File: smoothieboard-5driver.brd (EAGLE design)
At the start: 129.5 x 105.1 mm, 276 parts, among them IC1 LPC1769, IC10 LM1117-3.3V, IC11 78L12F, IC12 A4982, IC2 A4982, IC3 A4982, IC4 MCP44X1, IC5 A4982, IC6 A4982, IC9 MCP44X1, J10 POWER_JACKSMD, Q1 BSL207SP, Q10 SUD50P04-08-GE3, Q2 12MHz, Q3 25MHz, Q4 ZXMN4A06, Q5 AOT240L, Q6 AOT240L, Q7 AOT240L, Q8 ZXMN4A06, Q9 ZXMN4A06, U1 USD-SOCKETNEW, X14 USBPTH

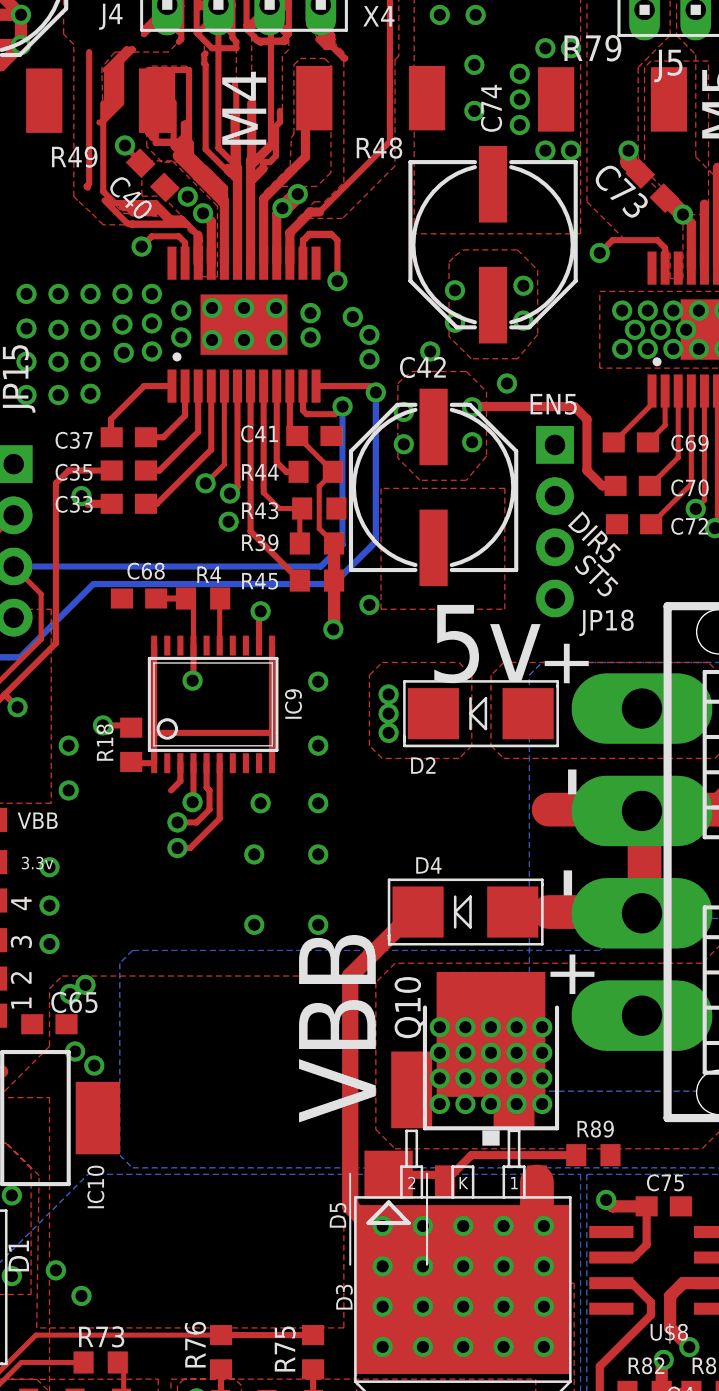
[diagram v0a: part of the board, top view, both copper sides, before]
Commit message: added footprint for optional R-78E-5.0 dc-dc converter for converting from VBB to 5V
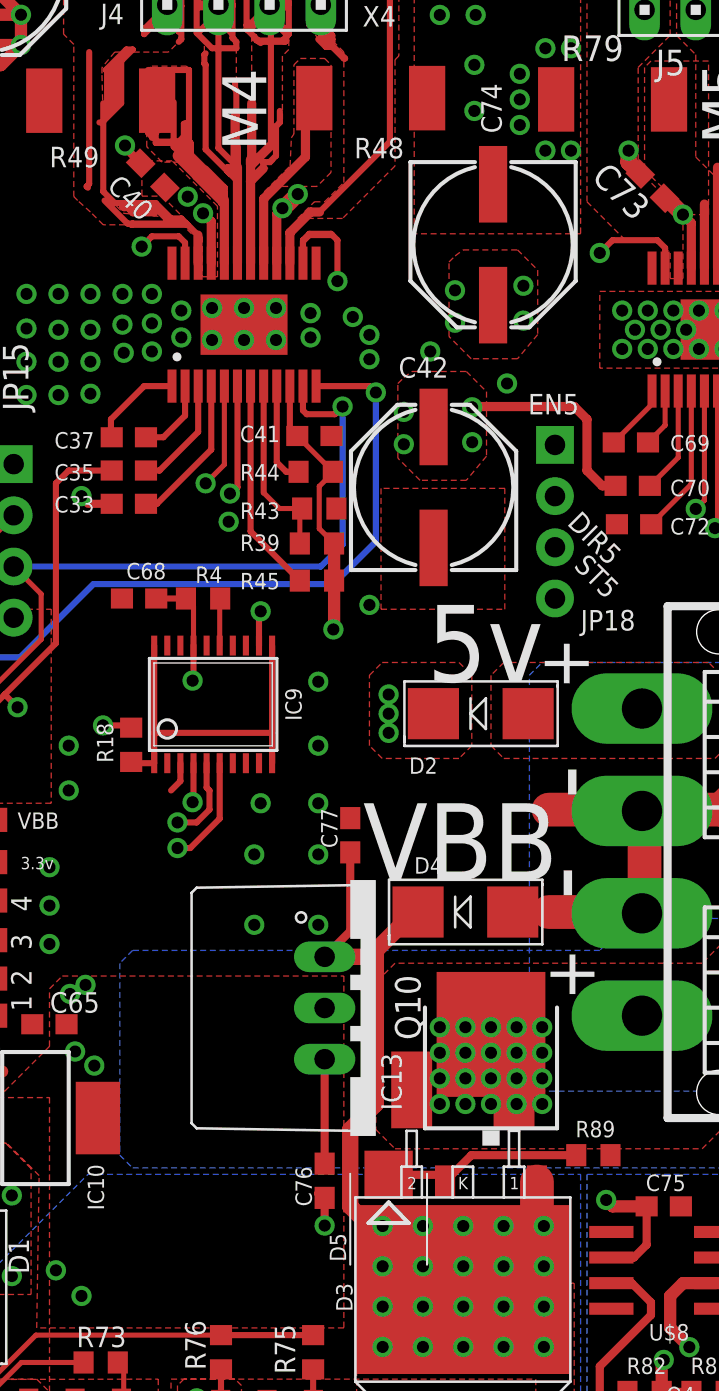
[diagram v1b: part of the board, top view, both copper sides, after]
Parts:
- added C76: .1uF, rcl:C0603
- added C77: .33uF, rcl:C0603
- added IC13: R-78E-5.0, logxen:R-78
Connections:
- net 5V: now also C76.1, IC13.3
- net GND: now also C76.2, C77.2, IC13.2
- net VBB: now also C77.1, IC13.1
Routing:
- net VBB: track 297.7 -> 306.1 mm
- net 5V: track 129.6 -> 137.8 mm
- net GND: track 286.5 -> 288.6 mm, vias 330 -> 331
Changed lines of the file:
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@@
 <?xml version="1.0" encoding="utf-8"?>
 <!DOCTYPE eagle SYSTEM "eagle.dtd">
-<eagle version="6.2">
+<eagle version="6.3">
 <drawing>
 <settings>
@@
 <grid distance="12.5" unitdist="mil" unit="mil" style="dots" multiple="8" display="no" altdistance="6.25" altunitdist="mil" altunit="mil"/>
 <layers>
-<layer number="1" name="Top" color="4" fill="1" visible="no" active="yes"/>
+<layer number="1" name="Top" color="4" fill="1" visible="yes" active="yes"/>
 <layer number="2" name="Route2" color="2" fill="1" visible="no" active="yes"/>
 <layer number="3" name="Route3" color="4" fill="3" visible="no" active="no"/>
@@
 <layer number="110" name="fp0" color="7" fill="1" visible="no" active="yes"/>
 <layer number="111" name="LPC17xx" color="7" fill="1" visible="no" active="yes"/>
+<layer number="112" name="tSilk" color="7" fill="1" visible="yes" active="yes"/>
 <layer number="116" name="Patch_BOT" color="9" fill="4" visible="no" active="yes"/>
 <layer number="121" name="_tsilk" color="7" fill="1" visible="yes" active="yes"/>
@@
 <layer number="124" name="bTestmark" color="7" fill="1" visible="no" active="yes"/>
 <layer number="125" name="_tNames" color="7" fill="1" visible="no" active="yes"/>
+<layer number="126" name="_bNames" color="7" fill="1" visible="yes" active="yes"/>
+<layer number="127" name="_tValues" color="7" fill="1" visible="yes" active="yes"/>
+<layer number="128" name="_bValues" color="7" fill="1" visible="yes" active="yes"/>
 <layer number="131" name="tAdjust" color="7" fill="1" visible="no" active="yes"/>
 <layer number="132" name="bAdjust" color="7" fill="1" visible="no" active="yes"/>
 <layer number="144" name="Drill_legend" color="7" fill="1" visible="no" active="yes"/>
 <layer number="151" name="HeatSink" color="7" fill="1" visible="no" active="yes"/>
+<layer number="152" name="_bDocu" color="7" fill="1" visible="yes" active="yes"/>
 <layer number="199" name="Contour" color="7" fill="1" visible="no" active="yes"/>
 <layer number="200" name="200bmp" color="1" fill="10" visible="no" active="yes"/>
@@
 <layer number="223" name="223bmp" color="24" fill="1" visible="no" active="no"/>
 <layer number="224" name="224bmp" color="25" fill="1" visible="no" active="no"/>
+<layer number="248" name="Housing" color="7" fill="1" visible="yes" active="yes"/>
+<layer number="249" name="Edge" color="7" fill="1" visible="yes" active="yes"/>
 <layer number="250" name="Descript" color="3" fill="1" visible="no" active="no"/>
 <layer number="251" name="SMDround" color="12" fill="11" visible="no" active="no"/>
@@
 <text x="107.886" y="68.255" size="1.016" layer="25" ratio="16" rot="R315">ST5</text>
 <text x="100.6475" y="62.5475" size="3.81" layer="121" ratio="16">5v</text>
-<text x="98.1075" y="40.64" size="3.81" layer="121" ratio="16" rot="R90">VBB</text>
+<text x="97.4725" y="52.705" size="3.81" layer="121" ratio="16">VBB</text>
 <text x="80.3275" y="55.245" size="0.8128" layer="121" ratio="16">VBB</text>
 <text x="18.0975" y="8.89" size="0.8128" layer="122" ratio="16" rot="MR270">5V</text>
@@
 </class>
 </classes>
-<designrules>
+<designrules name="default">
 <description language="de">&lt;b&gt;EAGLE Design Rules&lt;/b&gt;
 &lt;p&gt;
@@
 </element>
 <element name="D5" library="diode" package="SMB" value="15v" x="98.7425" y="35.8775" smashed="yes" rot="R270">
-<attribute name="NAME" x="95.8215" y="36.7665" size="0.8128" layer="25" rot="R270"/>
+<attribute name="NAME" x="95.8215" y="35.179" size="0.8128" layer="25" rot="R270"/>
 <attribute name="VALUE" x="95.3135" y="38.0365" size="1.27" layer="27" rot="R270"/>
 </element>
@@
 <attribute name="VALUE" x="75.8825" y="31.75" size="1.27" layer="27" rot="R180"/>
 </element>
+<element name="IC13" library="logxen" package="R-78" value="R-78E-5.0" x="98.1075" y="46.355" smashed="yes" rot="R270">
+<attribute name="NAME" x="99.3902" y="41.275" size="1.016" layer="25" ratio="10" rot="R90"/>
+<attribute name="VALUE" x="89.2175" y="52.705" size="1.27" layer="27" ratio="10"/>
+</element>
+<element name="C76" library="rcl" package="C0603" value=".1uF" x="95.5675" y="37.7825" smashed="yes" rot="R270">
+<attribute name="NAME" x="94.9325" y="36.5125" size="0.8128" layer="25" rot="R90"/>
+<attribute name="VALUE" x="93.6625" y="38.4175" size="1.27" layer="27" rot="R270"/>
+</element>
+<element name="C77" library="rcl" package="C0603" value=".33uF" x="96.8375" y="54.9275" smashed="yes" rot="R90">
+<attribute name="NAME" x="96.2025" y="54.2925" size="0.8128" layer="25" rot="R90"/>
+<attribute name="VALUE" x="98.7425" y="54.2925" size="1.27" layer="27" rot="R90"/>
+</element>
 </elements>
 <signals>
@@
 <contactref element="JP33" pad="5"/>
 <wire x1="76.975" y1="31.115" x2="74.6125" y2="31.115" width="0.8128" layer="15"/>
-<wire x1="86.43885625" y1="88.275940625" x2="85.6615" y2="89.154" width="0.254" layer="1"/>
+<contactref element="IC13" pad="2"/>
+<contactref element="C77" pad="2"/>
+<contactref element="C76" pad="2"/>
+<wire x1="86.43885625" y1="88.275940625" x2="85.6615" y2="89.053296875" width="0.4064" layer="1"/>
+<wire x1="85.6615" y1="89.053296875" x2="85.6615" y2="89.154" width="0.4064" layer="1"/>
+<wire x1="95.5675" y1="36.9325" x2="95.3525" y2="37.1475" width="0.4064" layer="1"/>
+<wire x1="95.3525" y1="37.1475" x2="95.25" y2="37.1475" width="0.4064" layer="1"/>
+<wire x1="95.25" y1="37.1475" x2="95.5675" y2="36.83" width="0.4064" layer="1"/>
+<wire x1="95.5675" y1="36.83" x2="95.5675" y2="35.56" width="0.4064" layer="1"/>
+<via x="95.5675" y="35.56" extent="1-16" drill="0.6"/>
 </signal>
 <signal name="3.3V">
@@
 <contactref element="D4" pad="C"/>
 <wire x1="100.203" y1="51.1175" x2="100.0125" y2="51.1175" width="0.8128" layer="1"/>
-<wire x1="100.0125" y1="51.1175" x2="96.8375" y2="47.9425" width="0.8128" layer="1"/>
-<wire x1="96.8375" y1="47.9425" x2="96.8375" y2="36.51" width="0.8128" layer="1"/>
+<wire x1="100.0125" y1="51.1175" x2="98.1075" y2="49.2125" width="0.8128" layer="1"/>
+<wire x1="98.1075" y1="49.2125" x2="98.1075" y2="41.5925" width="0.8128" layer="1"/>
+<wire x1="98.1075" y1="41.5925" x2="96.8375" y2="40.3225" width="0.8128" layer="1"/>
+<wire x1="96.8375" y1="40.3225" x2="96.8375" y2="36.51" width="0.8128" layer="1"/>
 <contactref element="Q10" pad="2"/>
 <contactref element="D5" pad="A"/>
@@
 <wire x1="98.445" y1="35.5375" x2="97.81" y2="35.5375" width="0.8128" layer="1"/>
 <wire x1="97.81" y1="35.5375" x2="96.8375" y2="36.51" width="0.8128" layer="1"/>
+<contactref element="IC13" pad="1"/>
+<contactref element="C77" pad="1"/>
+<wire x1="96.8375" y1="54.0775" x2="96.8375" y2="50.165" width="0.4064" layer="1"/>
+<wire x1="96.8375" y1="50.165" x2="95.5675" y2="48.895" width="0.4064" layer="1"/>
+<wire x1="98.1075" y1="49.2125" x2="97.79" y2="48.895" width="0.8128" layer="1"/>
+<wire x1="97.79" y1="48.895" x2="95.5675" y2="48.895" width="0.8128" layer="1"/>
 </signal>
 <signal name="P0W">
@@
 <wire x1="87.249" y1="89.281" x2="88.4555" y2="89.281" width="0.3048" layer="1"/>
 <wire x1="88.4555" y1="89.281" x2="88.519" y2="89.2175" width="0.3048" layer="1"/>
-<wire x1="86.9315" y1="89.916" x2="86.995" y2="90.2335" width="0.254" layer="1"/>
+<wire x1="86.9315" y1="89.916" x2="86.9315" y2="90.17" width="0.4064" layer="1"/>
 </signal>
 <signal name="N$48">
@@
 <vertex x="97.79" y="62.865"/>
 </polygon>
-<wire x1="93.6625" y1="60.325" x2="93.6625" y2="37.689" width="0.8128" layer="15"/>
+<wire x1="93.6625" y1="60.325" x2="93.6625" y2="44.45" width="0.8128" layer="15"/>
+<wire x1="93.6625" y1="44.45" x2="93.6625" y2="43.18" width="0.8128" layer="15"/>
+<wire x1="93.6625" y1="43.18" x2="93.6625" y2="37.689" width="0.8128" layer="15"/>
 <wire x1="93.6625" y1="37.689" x2="93.0275" y2="37.054" width="0.8128" layer="15"/>
 <wire x1="93.0275" y1="37.054" x2="80.046" y2="37.054" width="0.8128" layer="15"/>
@@
 <wire x1="16.637" y1="10.6045" x2="16.637" y2="8.118" width="0.6096" layer="16"/>
 <wire x1="16.637" y1="8.118" x2="16.504" y2="7.985" width="0.6096" layer="16"/>
+<contactref element="IC13" pad="3"/>
+<contactref element="C76" pad="1"/>
+<wire x1="95.5675" y1="38.6325" x2="95.5675" y2="43.815" width="0.4064" layer="1"/>
+<wire x1="94.2975" y1="43.815" x2="93.6625" y2="43.18" width="0.8128" layer="15"/>
+<wire x1="95.5675" y1="43.815" x2="94.2975" y2="43.815" width="0.8128" layer="15"/>
+<wire x1="94.2975" y1="43.815" x2="93.6625" y2="44.45" width="0.8128" layer="15"/>
 </signal>
 <signal name="+5V">

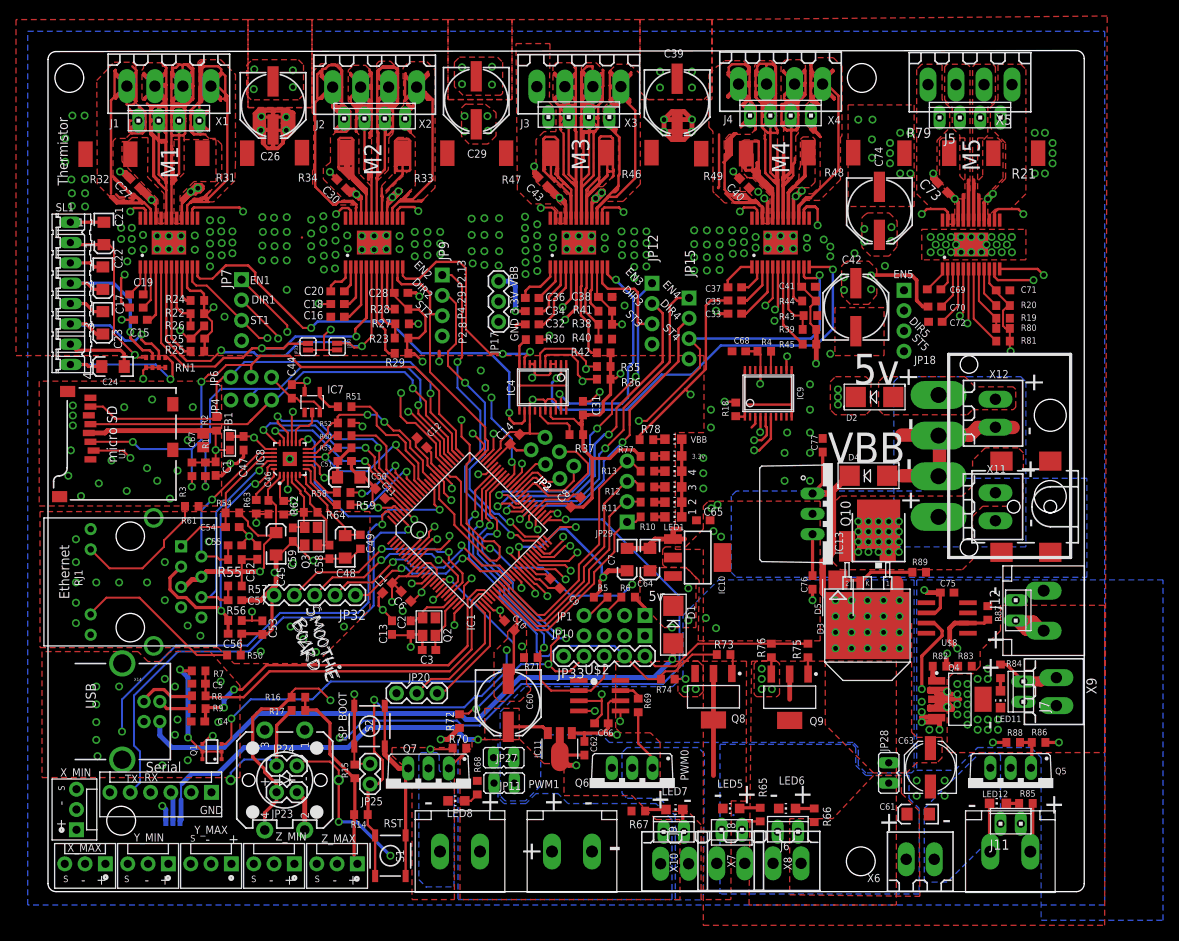
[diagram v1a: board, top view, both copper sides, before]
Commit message: add pull-downs on large mosfet gates, tons of silkscreen tidying including labelling of signals in connectors and power routing indicators
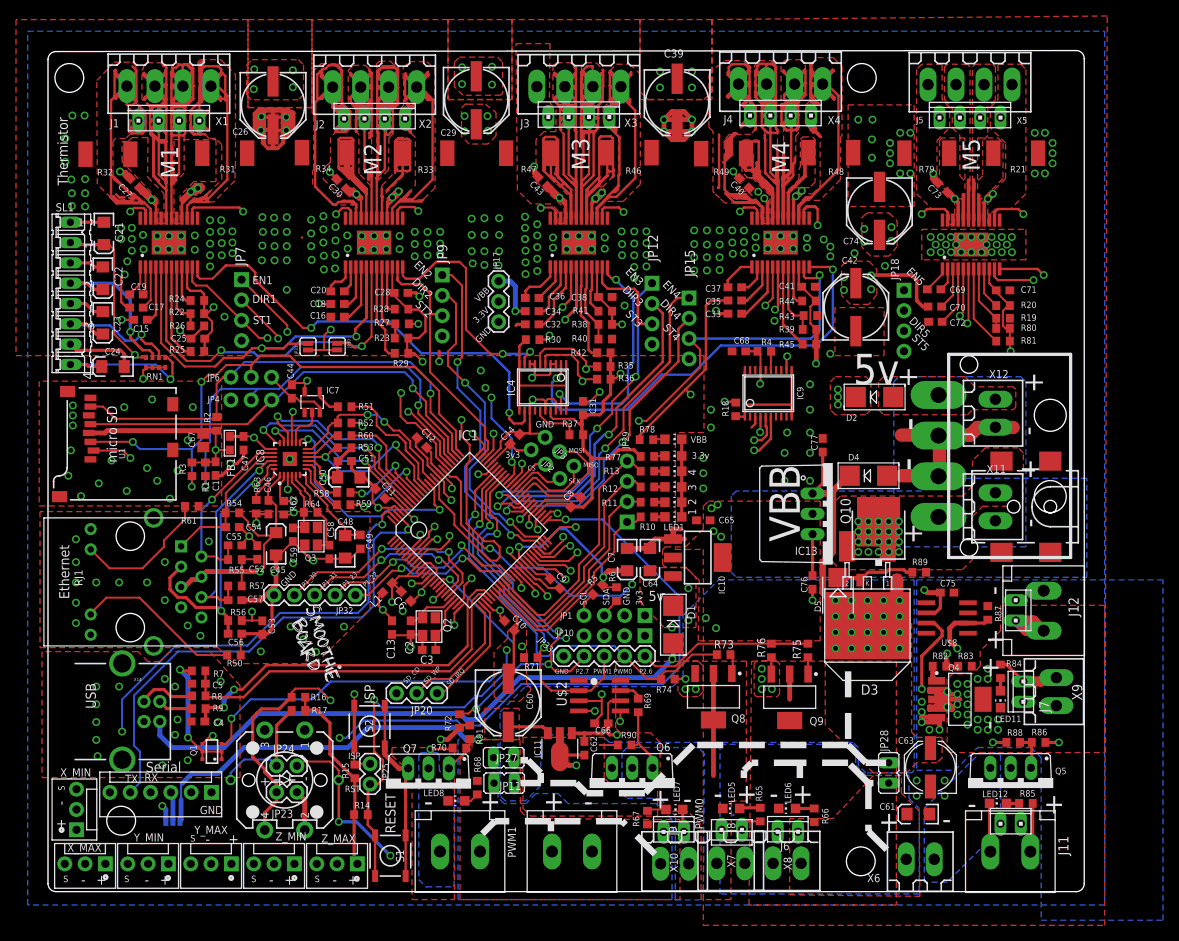
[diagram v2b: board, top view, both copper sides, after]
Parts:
- added R90, R91: 10k, resistor:R0603
- moved R6 1.51 mm to (71.1, 36.3), turned to 90 degrees
- moved R67 1.41 mm to (74.9, 8.38), turned to 90 degrees
- moved R5 1.02 mm to (68.7, 36.9), turned to 45 degrees
- moved D5 0.32 mm to (98.7, 36.2)
- moved Q10 0.32 mm to (103.8, 42.9)
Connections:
- net GND: now also R90.2, R91.2
- net GPIO_FET: now also R91.1
- net PWM1_FET: now also R90.1
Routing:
- net GND: track 288.6 -> 292.4 mm
- net 3.3V: track 301.2 -> 298.2 mm
- net GPIO_FET: track 3.44 -> 4.74 mm
- net PWM1_FET: track 7.69 -> 8.63 mm
- net SCL: track 44.8 -> 44.0 mm
- net SDA: track 50.6 -> 49.8 mm
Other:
- board text added: "3v3"
- board text added: "CS"
- board text added: "ISP"
- board text added: "MISO"
- board text added: "MOSI"
- board text added: "P1_22"
- board text added: "P1_23"
- board text added: "P1_30"
- board text added: "P1_31"
- board text added: "P2.6"
- board text added: "P2.7"
- board text added: "RESET"
- board text added: "SCK"
- board text added: "SCL"
- board text added: "SDA"
- board text added: "SD_CD"
- board text added: "SD_IRQ"
- board text added: "SD_WP"
- board text removed: "ISP_BOOT"
- board text removed: "P2.13"
- board text removed: "P2.8"
- board text removed: "P4.29"
